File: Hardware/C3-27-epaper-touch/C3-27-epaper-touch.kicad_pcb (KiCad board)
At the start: 4 copper layers, 70.2 x 71 mm, 61 parts, among them J1 AFC24-S24FIC-00, J2 USB_C_Programming, J3 Conn_01x06, J4 Conn_01x06_Female, J5 Groove sensor, Q1 Si1308, Q2 BC817, Q3 BC817, U1 ESP32-C3-WROOM-02-N4, U2 CP2102N-A02-GQFN28R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

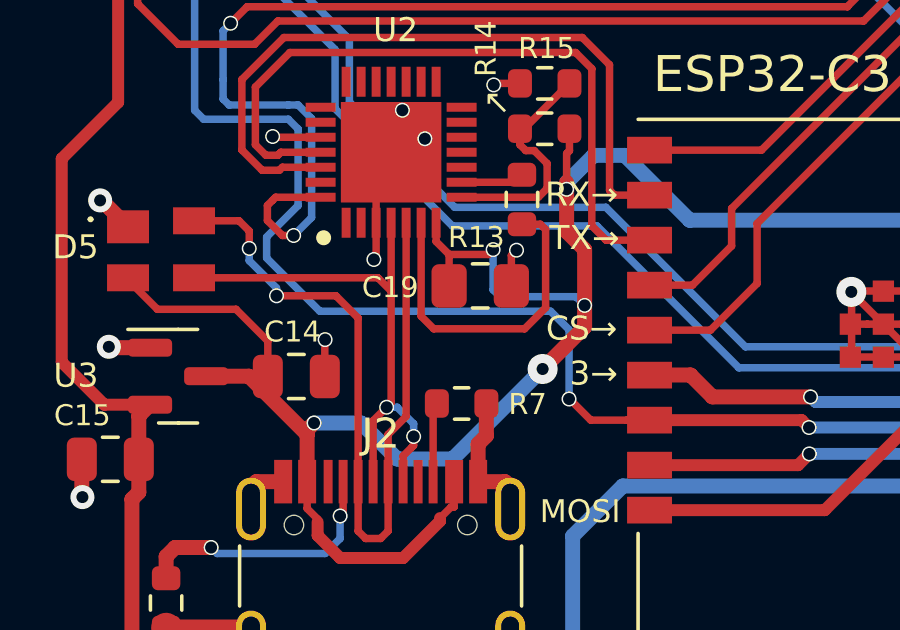
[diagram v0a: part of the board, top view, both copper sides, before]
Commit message: Revert "C3 1.1 remove C13 does not seem to be necessary (near CP2102)"
This reverts commit e9bbdf2bfd8dbd0aba68dd1d7c9680fb7645ba6f.
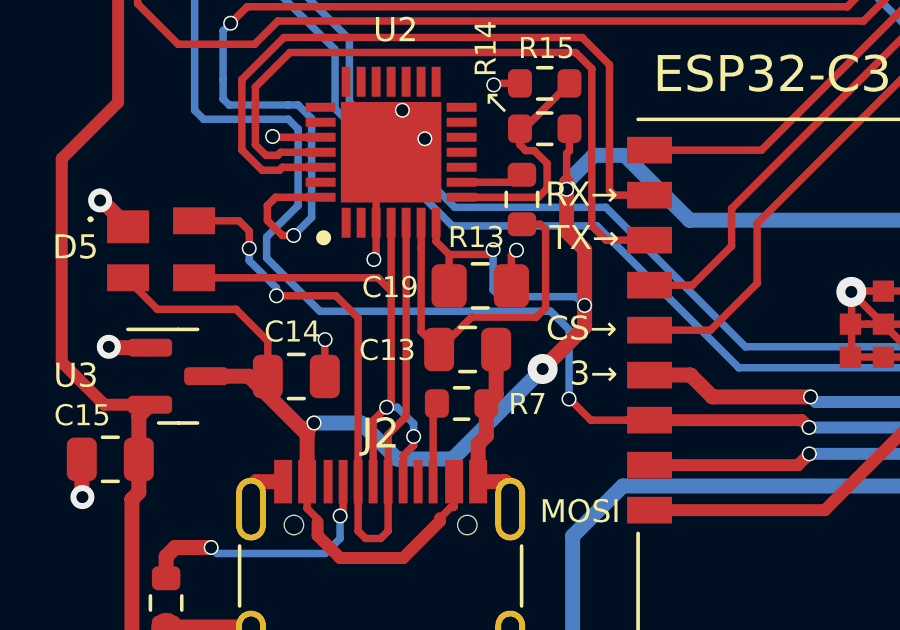
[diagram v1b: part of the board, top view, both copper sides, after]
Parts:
- added C13: 100nF, Capacitor_SMD:C_0805_2012Metric, F.Cu at (127.7, 112.3)
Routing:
- net GND: track 74.2 -> 76.1 mm
- net Net-(C13-Pad1): track 11.2 -> 12.1 mm
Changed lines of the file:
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@@
   (net 39 "Net-(Q2-Pad1)")
   (net 40 "/RTS")
-  (net 41 "Net-(R13-Pad1)")
+  (net 41 "Net-(C13-Pad1)")
   (net 42 "Net-(Q3-Pad1)")
   (net 43 "/DTR")
@@
     (fp_line (start 0.8 -0.4125) (end 0.8 0.4125) (layer "F.Fab") (width 0.1))
     (pad "1" smd roundrect (at -0.825 0 90) (size 0.8 0.95) (layers "F.Cu" "F.Paste" "F.Mask") (roundrect_rratio 0.25)
-      (net 41 "Net-(R13-Pad1)") (pintype "passive"))
+      (net 41 "Net-(C13-Pad1)") (pintype "passive"))
     (pad "2" smd roundrect (at 0.825 0 90) (size 0.8 0.95) (layers "F.Cu" "F.Paste" "F.Mask") (roundrect_rratio 0.25)
       (net 36 "Net-(R13-Pad2)") (pintype "passive"))
@@
     )
   )
+  (footprint "Capacitor_SMD:C_0805_2012Metric" (layer "F.Cu")
+    (at 127.7 112.3)
+    (descr "Capacitor SMD 0805 (2012 Metric), square (rectangular) end terminal, IPC_7351 nominal, (Body size source: IPC-SM-782 page 76, https://www.pcb-3d.com/wordpress/wp-content/uploads/ipc-sm-782a_amendment_1_and_2.pdf, https://docs.google.com/spreadsheets/d/1BsfQQcO9C6DZCsRaXUlFlo91Tg2WpOkGARC1WS5S8t0/edit?usp=sharing), generated with kicad-footprint-generator")
+    (tags "capacitor")
+    (property "LCSC" "C28233")
+    (property "Sheetfile" "C3-27-epaper-touch.kicad_sch")
+    (property "Sheetname" "")
+    (attr smd)
+    (fp_text reference "C13" (at -2.675 0.025 180) (layer "F.SilkS")
+      (effects (font (size 0.7 0.7) (thickness 0.13)))
+    )
+    (fp_text value "100nF" (at 0 1.68) (layer "F.Fab")
+      (effects (font (size 1 1) (thickness 0.15)))
+    )
+    (fp_text user "${REFERENCE}" (at 0 0) (layer "F.Fab")
+      (effects (font (size 0.5 0.5) (thickness 0.08)))
+    )
+    (fp_line (start -0.261252 0.735) (end 0.261252 0.735) (layer "F.SilkS") (width 0.12))
+    (fp_line (start -0.261252 -0.735) (end 0.261252 -0.735) (layer "F.SilkS") (width 0.12))
+    (fp_line (start 1.7 0.98) (end -1.7 0.98) (layer "F.CrtYd") (width 0.05))
+    (fp_line (start -1.7 -0.98) (end 1.7 -0.98) (layer "F.CrtYd") (width 0.05))
+    (fp_line (start 1.7 -0.98) (end 1.7 0.98) (layer "F.CrtYd") (width 0.05))
+    (fp_line (start -1.7 0.98) (end -1.7 -0.98) (layer "F.CrtYd") (width 0.05))
+    (fp_line (start -1 -0.625) (end 1 -0.625) (layer "F.Fab") (width 0.1))
+    (fp_line (start 1 -0.625) (end 1 0.625) (layer "F.Fab") (width 0.1))
+    (fp_line (start -1 0.625) (end -1 -0.625) (layer "F.Fab") (width 0.1))
+    (fp_line (start 1 0.625) (end -1 0.625) (layer "F.Fab") (width 0.1))
+    (pad "1" smd roundrect (at -0.95 0) (size 1 1.45) (layers "F.Cu" "F.Paste" "F.Mask") (roundrect_rratio 0.25)
+      (net 41 "Net-(C13-Pad1)") (pintype "passive"))
+    (pad "2" smd roundrect (at 0.95 0) (size 1 1.45) (layers "F.Cu" "F.Paste" "F.Mask") (roundrect_rratio 0.25)
+      (net 1 "GND") (pintype "passive"))
+    (model "${KICAD6_3DMODEL_DIR}/Capacitor_SMD.3dshapes/C_0805_2012Metric.wrl"
+      (offset (xyz 0 0 0))
+      (scale (xyz 1 1 1))
+      (rotate (xyz 0 0 0))
+    )
+  )
   (footprint "Resistor_SMD:R_0603_1608Metric" (layer "F.Cu")
     (at 120.01 98.18 -90)
@@
       (net 72 "/D-") (pinfunction "D-") (pintype "passive"))
     (pad "6" smd rect (at -2.35 1 180) (size 0.3 1) (layers "F.Cu" "F.Paste" "F.Mask")
-      (net 41 "Net-(R13-Pad1)") (pinfunction "VDD") (pintype "passive"))
+      (net 41 "Net-(C13-Pad1)") (pinfunction "VDD") (pintype "passive"))
     (pad "7" smd rect (at -2.35 1.5 180) (size 0.3 1) (layers "F.Cu" "F.Paste" "F.Mask")
       (net 3 "VBUS") (pinfunction "VREGIN") (pintype "passive"))
@@
   (segment (start 150.1375 90.8) (end 150.1375 92.0225) (width 0.5) (layer "F.Cu") (net 1))
   (segment (start 142.154888 111.455112) (end 141.024888 111.455112) (width 0.25) (layer "F.Cu") (net 1))
+  (segment (start 128.65 113.8) (end 128.65 112.3) (width 0.5) (layer "F.Cu") (net 1))
   (segment (start 158.3875 69.95) (end 157.15 69.95) (width 0.5) (layer "F.Cu") (net 1))
   (segment (start 155.7875 86.2625) (end 155.7875 85.65) (width 0.4) (layer "F.Cu") (net 1))
@@
   (segment (start 148.600001 78.825001) (end 148.05 78.275) (width 0.25) (layer "F.Cu") (net 1))
   (segment (start 140.5 112.55) (end 142.653088 112.55) (width 0.25) (layer "F.Cu") (net 1))
+  (segment (start 128.35 114.1) (end 128.65 113.8) (width 0.5) (layer "F.Cu") (net 1))
   (segment (start 153.7375 88.3125) (end 154.85 87.2) (width 0.4) (layer "F.Cu") (net 1))
   (segment (start 154.85 87.2) (end 155.7875 86.2625) (width 0.4) (layer "F.Cu") (net 1))
@@
   (segment (start 133.5 83.05) (end 134.625 81.925) (width 0.5) (layer "F.Cu") (net 1))
   (segment (start 141.024888 111.455112) (end 140.458299 111.455112) (width 0.25) (layer "F.Cu") (net 1))
+  (segment (start 128.325 114.1) (end 128.35 114.1) (width 0.5) (layer "F.Cu") (net 1))
   (segment (start 151.264 105.655085) (end 153.335085 105.655085) (width 0.5) (layer "F.Cu") (net 1))
   (segment (start 117.875 121.8) (end 117.65 121.575) (width 1) (layer "F.Cu") (net 1))
@@
   (segment (start 130.3 110.91) (end 130.3 108.3) (width 0.25) (layer "F.Cu") (net 41))
   (segment (start 130.3 108.3) (end 130.125 108.125) (width 0.25) (layer "F.Cu") (net 41))
-  (segment (start 129.6 111.61) (end 126.57 111.61) (width 0.25) (layer "F.Cu") (net 41))
-  (segment (start 126.15 111.19) (end 126.15 108.075) (width 0.25) (layer "F.Cu") (net 41))
-  (segment (start 130.3 110.91) (end 129.6 111.61) (width 0.25) (layer "F.Cu") (net 41))
-  (segment (start 126.57 111.61) (end 126.15 111.19) (width 0.25) (layer "F.Cu") (net 41))
+  (segment (start 126.15 111.7) (end 126.75 112.3) (width 0.25) (layer "F.Cu") (net 41))
+  (segment (start 126.15 108.075) (end 126.15 108.9) (width 0.25) (layer "F.Cu") (net 41))
+  (segment (start 127.83 111.22) (end 129.99 111.22) (width 0.25) (layer "F.Cu") (net 41))
+  (segment (start 126.75 112.3) (end 127.83 111.22) (width 0.25) (layer "F.Cu") (net 41))
+  (segment (start 129.99 111.22) (end 130.3 110.91) (width 0.25) (layer "F.Cu") (net 41))
+  (segment (start 126.15 108.9) (end 126.15 111.7) (width 0.25) (layer "F.Cu") (net 41))
   (segment (start 130.125 108.125) (end 129.51 108.125) (width 0.25) (layer "F.Cu") (net 41))
   (segment (start 150.2375 103.19) (end 152.075 103.19) (width 0.25) (layer "F.Cu") (net 42))

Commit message: C3 1.1 remove C13 does not seem to be necessary (near CP2102)
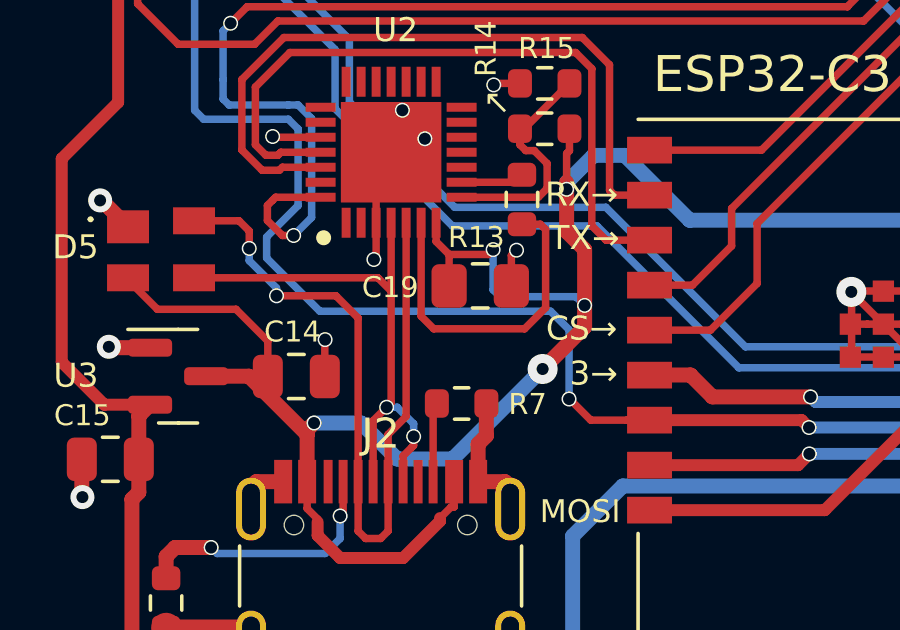
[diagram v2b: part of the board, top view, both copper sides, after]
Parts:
- removed C13: 100nF, Capacitor_SMD:C_0805_2012Metric
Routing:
- net GND: track 76.1 -> 74.2 mm
- net Net-(R13-Pad1): track 12.1 -> 11.2 mm
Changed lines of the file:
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@@
   (net 39 "Net-(Q2-Pad1)")
   (net 40 "/RTS")
-  (net 41 "Net-(C13-Pad1)")
+  (net 41 "Net-(R13-Pad1)")
   (net 42 "Net-(Q3-Pad1)")
   (net 43 "/DTR")
@@
     (fp_line (start 0.8 -0.4125) (end 0.8 0.4125) (layer "F.Fab") (width 0.1))
     (pad "1" smd roundrect (at -0.825 0 90) (size 0.8 0.95) (layers "F.Cu" "F.Paste" "F.Mask") (roundrect_rratio 0.25)
-      (net 41 "Net-(C13-Pad1)") (pintype "passive"))
+      (net 41 "Net-(R13-Pad1)") (pintype "passive"))
     (pad "2" smd roundrect (at 0.825 0 90) (size 0.8 0.95) (layers "F.Cu" "F.Paste" "F.Mask") (roundrect_rratio 0.25)
       (net 36 "Net-(R13-Pad2)") (pintype "passive"))
@@
     )
   )
-  (footprint "Capacitor_SMD:C_0805_2012Metric" (layer "F.Cu")
-    (at 127.7 112.3)
-    (descr "Capacitor SMD 0805 (2012 Metric), square (rectangular) end terminal, IPC_7351 nominal, (Body size source: IPC-SM-782 page 76, https://www.pcb-3d.com/wordpress/wp-content/uploads/ipc-sm-782a_amendment_1_and_2.pdf, https://docs.google.com/spreadsheets/d/1BsfQQcO9C6DZCsRaXUlFlo91Tg2WpOkGARC1WS5S8t0/edit?usp=sharing), generated with kicad-footprint-generator")
-    (tags "capacitor")
-    (property "LCSC" "C28233")
-    (property "Sheetfile" "C3-27-epaper-touch.kicad_sch")
-    (property "Sheetname" "")
-    (attr smd)
-    (fp_text reference "C13" (at -2.675 0.025 180) (layer "F.SilkS")
-      (effects (font (size 0.7 0.7) (thickness 0.13)))
-    )
-    (fp_text value "100nF" (at 0 1.68) (layer "F.Fab")
-      (effects (font (size 1 1) (thickness 0.15)))
-    )
-    (fp_text user "${REFERENCE}" (at 0 0) (layer "F.Fab")
-      (effects (font (size 0.5 0.5) (thickness 0.08)))
-    )
-    (fp_line (start -0.261252 0.735) (end 0.261252 0.735) (layer "F.SilkS") (width 0.12))
-    (fp_line (start -0.261252 -0.735) (end 0.261252 -0.735) (layer "F.SilkS") (width 0.12))
-    (fp_line (start 1.7 0.98) (end -1.7 0.98) (layer "F.CrtYd") (width 0.05))
-    (fp_line (start -1.7 -0.98) (end 1.7 -0.98) (layer "F.CrtYd") (width 0.05))
-    (fp_line (start 1.7 -0.98) (end 1.7 0.98) (layer "F.CrtYd") (width 0.05))
-    (fp_line (start -1.7 0.98) (end -1.7 -0.98) (layer "F.CrtYd") (width 0.05))
-    (fp_line (start -1 -0.625) (end 1 -0.625) (layer "F.Fab") (width 0.1))
-    (fp_line (start 1 -0.625) (end 1 0.625) (layer "F.Fab") (width 0.1))
-    (fp_line (start -1 0.625) (end -1 -0.625) (layer "F.Fab") (width 0.1))
-    (fp_line (start 1 0.625) (end -1 0.625) (layer "F.Fab") (width 0.1))
-    (pad "1" smd roundrect (at -0.95 0) (size 1 1.45) (layers "F.Cu" "F.Paste" "F.Mask") (roundrect_rratio 0.25)
-      (net 41 "Net-(C13-Pad1)") (pintype "passive"))
-    (pad "2" smd roundrect (at 0.95 0) (size 1 1.45) (layers "F.Cu" "F.Paste" "F.Mask") (roundrect_rratio 0.25)
-      (net 1 "GND") (pintype "passive"))
-    (model "${KICAD6_3DMODEL_DIR}/Capacitor_SMD.3dshapes/C_0805_2012Metric.wrl"
-      (offset (xyz 0 0 0))
-      (scale (xyz 1 1 1))
-      (rotate (xyz 0 0 0))
-    )
-  )
   (footprint "Resistor_SMD:R_0603_1608Metric" (layer "F.Cu")
     (at 120.01 98.18 -90)
@@
       (net 72 "/D-") (pinfunction "D-") (pintype "passive"))
     (pad "6" smd rect (at -2.35 1 180) (size 0.3 1) (layers "F.Cu" "F.Paste" "F.Mask")
-      (net 41 "Net-(C13-Pad1)") (pinfunction "VDD") (pintype "passive"))
+      (net 41 "Net-(R13-Pad1)") (pinfunction "VDD") (pintype "passive"))
     (pad "7" smd rect (at -2.35 1.5 180) (size 0.3 1) (layers "F.Cu" "F.Paste" "F.Mask")
       (net 3 "VBUS") (pinfunction "VREGIN") (pintype "passive"))
@@
   (segment (start 150.1375 90.8) (end 150.1375 92.0225) (width 0.5) (layer "F.Cu") (net 1))
   (segment (start 142.154888 111.455112) (end 141.024888 111.455112) (width 0.25) (layer "F.Cu") (net 1))
-  (segment (start 128.65 113.8) (end 128.65 112.3) (width 0.5) (layer "F.Cu") (net 1))
   (segment (start 158.3875 69.95) (end 157.15 69.95) (width 0.5) (layer "F.Cu") (net 1))
   (segment (start 155.7875 86.2625) (end 155.7875 85.65) (width 0.4) (layer "F.Cu") (net 1))
@@
   (segment (start 148.600001 78.825001) (end 148.05 78.275) (width 0.25) (layer "F.Cu") (net 1))
   (segment (start 140.5 112.55) (end 142.653088 112.55) (width 0.25) (layer "F.Cu") (net 1))
-  (segment (start 128.35 114.1) (end 128.65 113.8) (width 0.5) (layer "F.Cu") (net 1))
   (segment (start 153.7375 88.3125) (end 154.85 87.2) (width 0.4) (layer "F.Cu") (net 1))
   (segment (start 154.85 87.2) (end 155.7875 86.2625) (width 0.4) (layer "F.Cu") (net 1))
@@
   (segment (start 133.5 83.05) (end 134.625 81.925) (width 0.5) (layer "F.Cu") (net 1))
   (segment (start 141.024888 111.455112) (end 140.458299 111.455112) (width 0.25) (layer "F.Cu") (net 1))
-  (segment (start 128.325 114.1) (end 128.35 114.1) (width 0.5) (layer "F.Cu") (net 1))
   (segment (start 151.264 105.655085) (end 153.335085 105.655085) (width 0.5) (layer "F.Cu") (net 1))
   (segment (start 117.875 121.8) (end 117.65 121.575) (width 1) (layer "F.Cu") (net 1))
@@
   (segment (start 130.3 110.91) (end 130.3 108.3) (width 0.25) (layer "F.Cu") (net 41))
   (segment (start 130.3 108.3) (end 130.125 108.125) (width 0.25) (layer "F.Cu") (net 41))
-  (segment (start 126.15 111.7) (end 126.75 112.3) (width 0.25) (layer "F.Cu") (net 41))
-  (segment (start 126.15 108.075) (end 126.15 108.9) (width 0.25) (layer "F.Cu") (net 41))
-  (segment (start 127.83 111.22) (end 129.99 111.22) (width 0.25) (layer "F.Cu") (net 41))
-  (segment (start 126.75 112.3) (end 127.83 111.22) (width 0.25) (layer "F.Cu") (net 41))
-  (segment (start 129.99 111.22) (end 130.3 110.91) (width 0.25) (layer "F.Cu") (net 41))
-  (segment (start 126.15 108.9) (end 126.15 111.7) (width 0.25) (layer "F.Cu") (net 41))
+  (segment (start 129.6 111.61) (end 126.57 111.61) (width 0.25) (layer "F.Cu") (net 41))
+  (segment (start 126.15 111.19) (end 126.15 108.075) (width 0.25) (layer "F.Cu") (net 41))
+  (segment (start 130.3 110.91) (end 129.6 111.61) (width 0.25) (layer "F.Cu") (net 41))
+  (segment (start 126.57 111.61) (end 126.15 111.19) (width 0.25) (layer "F.Cu") (net 41))
   (segment (start 130.125 108.125) (end 129.51 108.125) (width 0.25) (layer "F.Cu") (net 41))
   (segment (start 150.2375 103.19) (end 152.075 103.19) (width 0.25) (layer "F.Cu") (net 42))
